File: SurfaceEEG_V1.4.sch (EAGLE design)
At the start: 71 parts, among them IC1 LMV602, IC2 TSZ124IQ4T, U1 MCP4442-103E/ST, U2 ATMEGA328P-MU, U3 NRF24L01ALT1

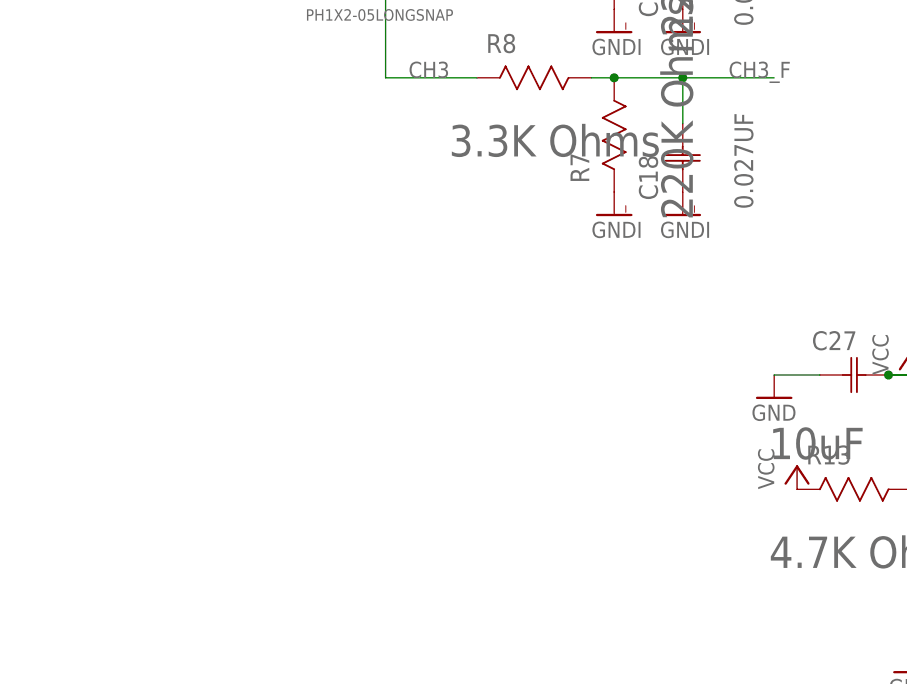
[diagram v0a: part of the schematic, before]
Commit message: Added active ground
Ku = 50 dB on 50 Hz
A low-pass filter = -6 dB/octave, 1 kHz = 26 dB, 22 kHz = 0 dB
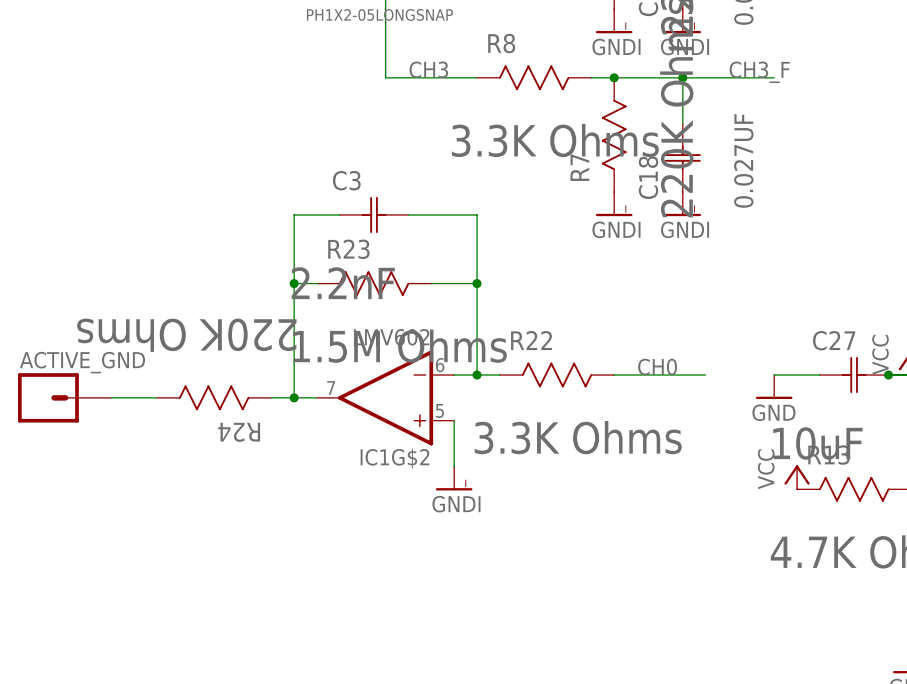
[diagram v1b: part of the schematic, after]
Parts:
- added ACTIVE_GND: (no value), SparkFun-Connectors:M01PTH
- added C3: 2.2nF, (manufact)-Kemet-element14:C0402C222K5RACTU
- added R22: 3.3K Ohms, (manufact)-resistors-YAGEO-element14:RC0603FR-073K3L
- added R23: 1.5M Ohms, (manufact)-resistors-YAGEO-element14:RC0603FR-071M5L
- added R24: 220K Ohms, (manufact)-resistors-YAGEO-element14:RC0603FR-07220KL
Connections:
- new net N$10: ACTIVE_GND.1, R24.R1
- new net N$3: C3.C2, IC1G$2.IN-, R22.R2, R23.R1
- new net N$6: C3.C1, IC1G$2.OUT, R23.R2, R24.R2
- net CH0: now also R22.R1
- net GNDI: now also IC1G$2.IN+
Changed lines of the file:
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@@
 <part name="R20" library="(manufact)-resistors-YAGEO-element14" deviceset="RT0603FRE0782KL" device="" value="88.7K EDIT"/>
 <part name="P+3" library="supply1" deviceset="VCC" device=""/>
+<part name="R22" library="(manufact)-resistors-YAGEO-element14" deviceset="RC0603FR-073K3L" device="" value="3.3K Ohms"/>
+<part name="GNDI20" library="supply1" deviceset="GNDI" device=""/>
+<part name="R23" library="(manufact)-resistors-YAGEO-element14" deviceset="RC0603FR-071M5L" device="" value="1.5M Ohms"/>
+<part name="R24" library="(manufact)-resistors-YAGEO-element14" deviceset="RC0603FR-07220KL" device="" value="220K Ohms"/>
+<part name="C3" library="(manufact)-Kemet-element14" deviceset="C0402C222K5RACTU" device="" value="2.2nF"/>
+<part name="ACTIVE_GND" library="SparkFun-Connectors" deviceset="M01" device="PTH"/>
 </parts>
 <sheets>
@@
 <instance part="R20" gate="A" x="86.36" y="114.3"/>
 <instance part="P+3" gate="VCC" x="99.06" y="116.84"/>
+<instance part="IC1" gate="G$2" x="-129.54" y="63.5" rot="R180"/>
+<instance part="R22" gate="A" x="-116.84" y="66.04"/>
+<instance part="GNDI20" gate="G$1" x="-121.92" y="53.34"/>
+<instance part="R23" gate="A" x="-137.16" y="76.2"/>
+<instance part="R24" gate="A" x="-142.24" y="63.5" rot="R180"/>
+<instance part="C3" gate="A" x="-134.62" y="83.82"/>
+<instance part="ACTIVE_GND" gate="G$1" x="-167.64" y="63.5"/>
 </instances>
 <busses>
@@
 <wire x1="-129.54" y1="160.02" x2="-129.54" y2="152.4" width="0.1524" layer="91"/>
 </segment>
+<segment>
+<wire x1="-93.98" y1="66.04" x2="-104.14" y2="66.04" width="0.1524" layer="91"/>
+<pinref part="R22" gate="A" pin="R1"/>
+<label x="-101.6" y="66.04" size="1.778" layer="95"/>
+</segment>
 </net>
 <net name="CH1" class="0">
@@
 <wire x1="-15.24" y1="193.04" x2="-7.62" y2="193.04" width="0.1524" layer="91"/>
 <pinref part="PH4" gate="G$1" pin="2"/>
+</segment>
+<segment>
+<pinref part="IC1" gate="G$2" pin="IN+"/>
+<pinref part="GNDI20" gate="G$1" pin="GNDI"/>
+<wire x1="-121.92" y1="55.88" x2="-121.92" y2="60.96" width="0.1524" layer="91"/>
 </segment>
 </net>
@@
 </segment>
 </net>
+<net name="N$3" class="0">
+<segment>
+<pinref part="IC1" gate="G$2" pin="IN-"/>
+<pinref part="R22" gate="A" pin="R2"/>
+<wire x1="-121.92" y1="66.04" x2="-119.38" y2="66.04" width="0.1524" layer="91"/>
+<pinref part="R23" gate="A" pin="R1"/>
+<wire x1="-119.38" y1="66.04" x2="-116.84" y2="66.04" width="0.1524" layer="91"/>
+<wire x1="-124.46" y1="76.2" x2="-119.38" y2="76.2" width="0.1524" layer="91"/>
+<wire x1="-119.38" y1="76.2" x2="-119.38" y2="66.04" width="0.1524" layer="91"/>
+<junction x="-119.38" y="66.04"/>
+<wire x1="-119.38" y1="76.2" x2="-119.38" y2="83.82" width="0.1524" layer="91"/>
+<junction x="-119.38" y="76.2"/>
+<wire x1="-119.38" y1="83.82" x2="-127" y2="83.82" width="0.1524" layer="91"/>
+<pinref part="C3" gate="A" pin="C2"/>
+</segment>
+</net>
+<net name="N$6" class="0">
+<segment>
+<pinref part="IC1" gate="G$2" pin="OUT"/>
+<wire x1="-137.16" y1="63.5" x2="-139.7" y2="63.5" width="0.1524" layer="91"/>
+<wire x1="-139.7" y1="63.5" x2="-139.7" y2="76.2" width="0.1524" layer="91"/>
+<pinref part="R23" gate="A" pin="R2"/>
+<wire x1="-139.7" y1="76.2" x2="-137.16" y2="76.2" width="0.1524" layer="91"/>
+<pinref part="R24" gate="A" pin="R2"/>
+<wire x1="-142.24" y1="63.5" x2="-139.7" y2="63.5" width="0.1524" layer="91"/>
+<junction x="-139.7" y="63.5"/>
+<wire x1="-139.7" y1="76.2" x2="-139.7" y2="83.82" width="0.1524" layer="91"/>
+<junction x="-139.7" y="76.2"/>
+<wire x1="-139.7" y1="83.82" x2="-134.62" y2="83.82" width="0.1524" layer="91"/>
+<pinref part="C3" gate="A" pin="C1"/>
+</segment>
+</net>
+<net name="N$10" class="0">
+<segment>
+<pinref part="R24" gate="A" pin="R1"/>
+<wire x1="-154.94" y1="63.5" x2="-160.02" y2="63.5" width="0.1524" layer="91"/>
+<pinref part="ACTIVE_GND" gate="G$1" pin="1"/>
+</segment>
+</net>

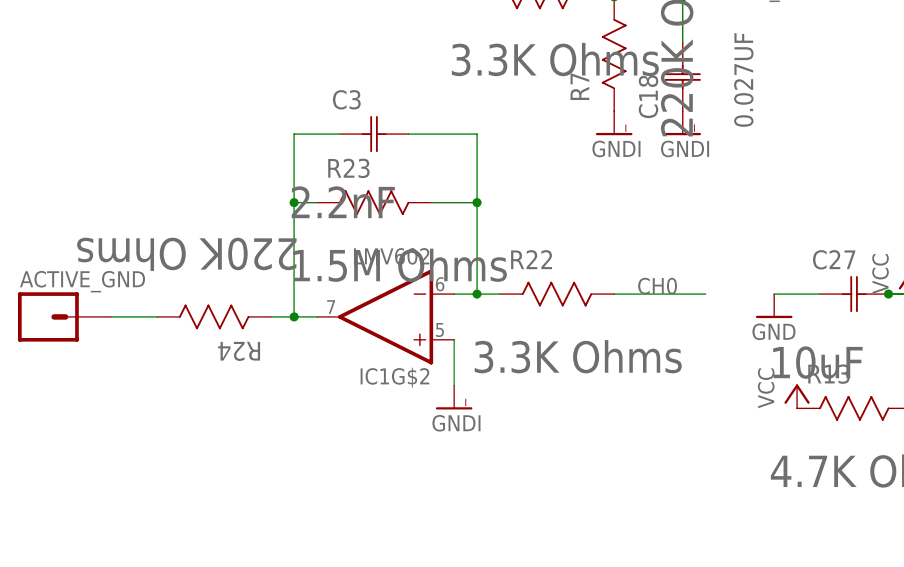
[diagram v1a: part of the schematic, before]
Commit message: Module active ground completed
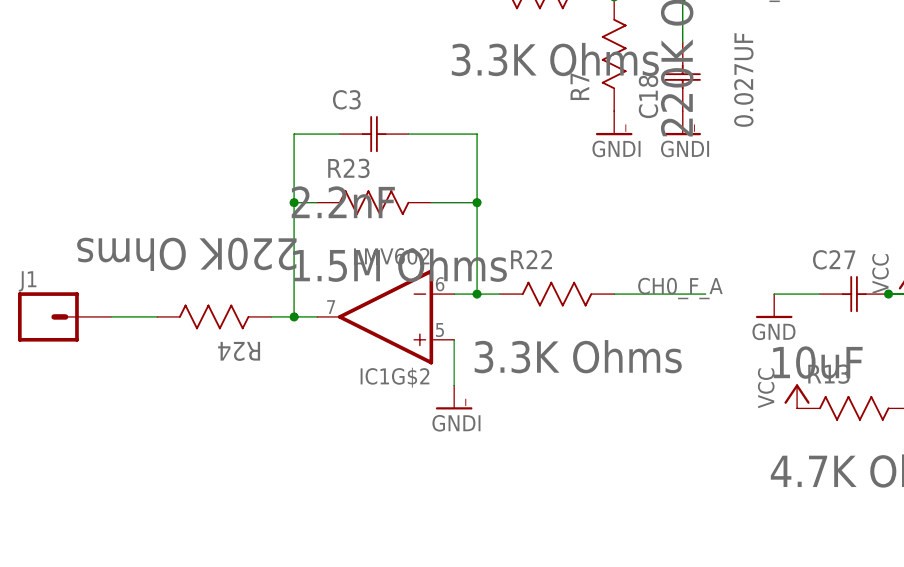
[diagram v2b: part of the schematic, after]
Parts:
- removed ACTIVE_GND: (no value), SparkFun-Connectors:M01PTH
- added J1: (no value), SparkFun-Connectors:M01SMD-4.5X1.5
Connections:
- net CH0: no longer R22.R1
- net CH0_F_A: now also R22.R1
- net N$10: now also J1.1; no longer ACTIVE_GND.1
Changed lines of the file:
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@@
 <part name="R24" library="(manufact)-resistors-YAGEO-element14" deviceset="RC0603FR-07220KL" device="" value="220K Ohms"/>
 <part name="C3" library="(manufact)-Kemet-element14" deviceset="C0402C222K5RACTU" device="" value="2.2nF"/>
-<part name="ACTIVE_GND" library="SparkFun-Connectors" deviceset="M01" device="PTH"/>
+<part name="J1" library="SparkFun-Connectors" deviceset="M01" device="SMD-4.5X1.5"/>
 </parts>
 <sheets>
@@
 <instance part="R24" gate="A" x="-142.24" y="63.5" rot="R180"/>
 <instance part="C3" gate="A" x="-134.62" y="83.82"/>
-<instance part="ACTIVE_GND" gate="G$1" x="-167.64" y="63.5"/>
+<instance part="J1" gate="G$1" x="-167.64" y="63.5"/>
 </instances>
 <busses>
@@
 <wire x1="-129.54" y1="160.02" x2="-129.54" y2="152.4" width="0.1524" layer="91"/>
 </segment>
-<segment>
-<wire x1="-93.98" y1="66.04" x2="-104.14" y2="66.04" width="0.1524" layer="91"/>
-<pinref part="R22" gate="A" pin="R1"/>
-<label x="-101.6" y="66.04" size="1.778" layer="95"/>
-</segment>
 </net>
 <net name="CH1" class="0">
@@
 <label x="20.32" y="104.14" size="1.778" layer="95"/>
 <pinref part="U$3" gate="G$1" pin="IN2+"/>
+</segment>
+<segment>
+<wire x1="-93.98" y1="66.04" x2="-104.14" y2="66.04" width="0.1524" layer="91"/>
+<pinref part="R22" gate="A" pin="R1"/>
+<label x="-101.6" y="66.04" size="1.778" layer="95"/>
 </segment>
 </net>
@@
 <pinref part="R24" gate="A" pin="R1"/>
 <wire x1="-154.94" y1="63.5" x2="-160.02" y2="63.5" width="0.1524" layer="91"/>
-<pinref part="ACTIVE_GND" gate="G$1" pin="1"/>
-</segment>
-</net>
+<pinref part="J1" gate="G$1" pin="1"/>
+</segment>
+</net>

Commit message: Board changed after library changes
After making fonts smaller, the board have changed
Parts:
- R19, R20: value 88.7K EDIT -> 82K Ohms
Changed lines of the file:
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@@
 <part name="R1" library="(manufact)-resistors-YAGEO-element14" deviceset="RC0603FR-0722KL" device="" value="22K Ohms"/>
 <part name="R2" library="(manufact)-resistors-YAGEO-element14" deviceset="RC0603FR-0720KL" device="" value="20K Ohms"/>
-<part name="R19" library="(manufact)-resistors-YAGEO-element14" deviceset="RT0603FRE0782KL" device="" value="88.7K EDIT"/>
+<part name="R19" library="(manufact)-resistors-YAGEO-element14" deviceset="RT0603FRE0782KL" device="" value="82K Ohms"/>
 <part name="C11" library="(manufact)-capacitors-AVX-element14" deviceset="UQCL2A150JAT2A/500" device="" value="15pF"/>
 <part name="C12" library="(manufact)-capacitors-AVX-element14" deviceset="UQCL2A150JAT2A/500" device="" value="15pF"/>
@@
 <part name="GND9" library="supply1" deviceset="GND" device=""/>
 <part name="GND11" library="supply1" deviceset="GND" device=""/>
-<part name="R20" library="(manufact)-resistors-YAGEO-element14" deviceset="RT0603FRE0782KL" device="" value="88.7K EDIT"/>
+<part name="R20" library="(manufact)-resistors-YAGEO-element14" deviceset="RT0603FRE0782KL" device="" value="82K Ohms"/>
 <part name="P+3" library="supply1" deviceset="VCC" device=""/>
 <part name="R22" library="(manufact)-resistors-YAGEO-element14" deviceset="RC0603FR-073K3L" device="" value="3.3K Ohms"/>
